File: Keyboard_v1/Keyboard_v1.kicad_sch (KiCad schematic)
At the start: 16 parts, among them SW1 SW_Push, U1 ATmega32U4-A, Y1 16MHz

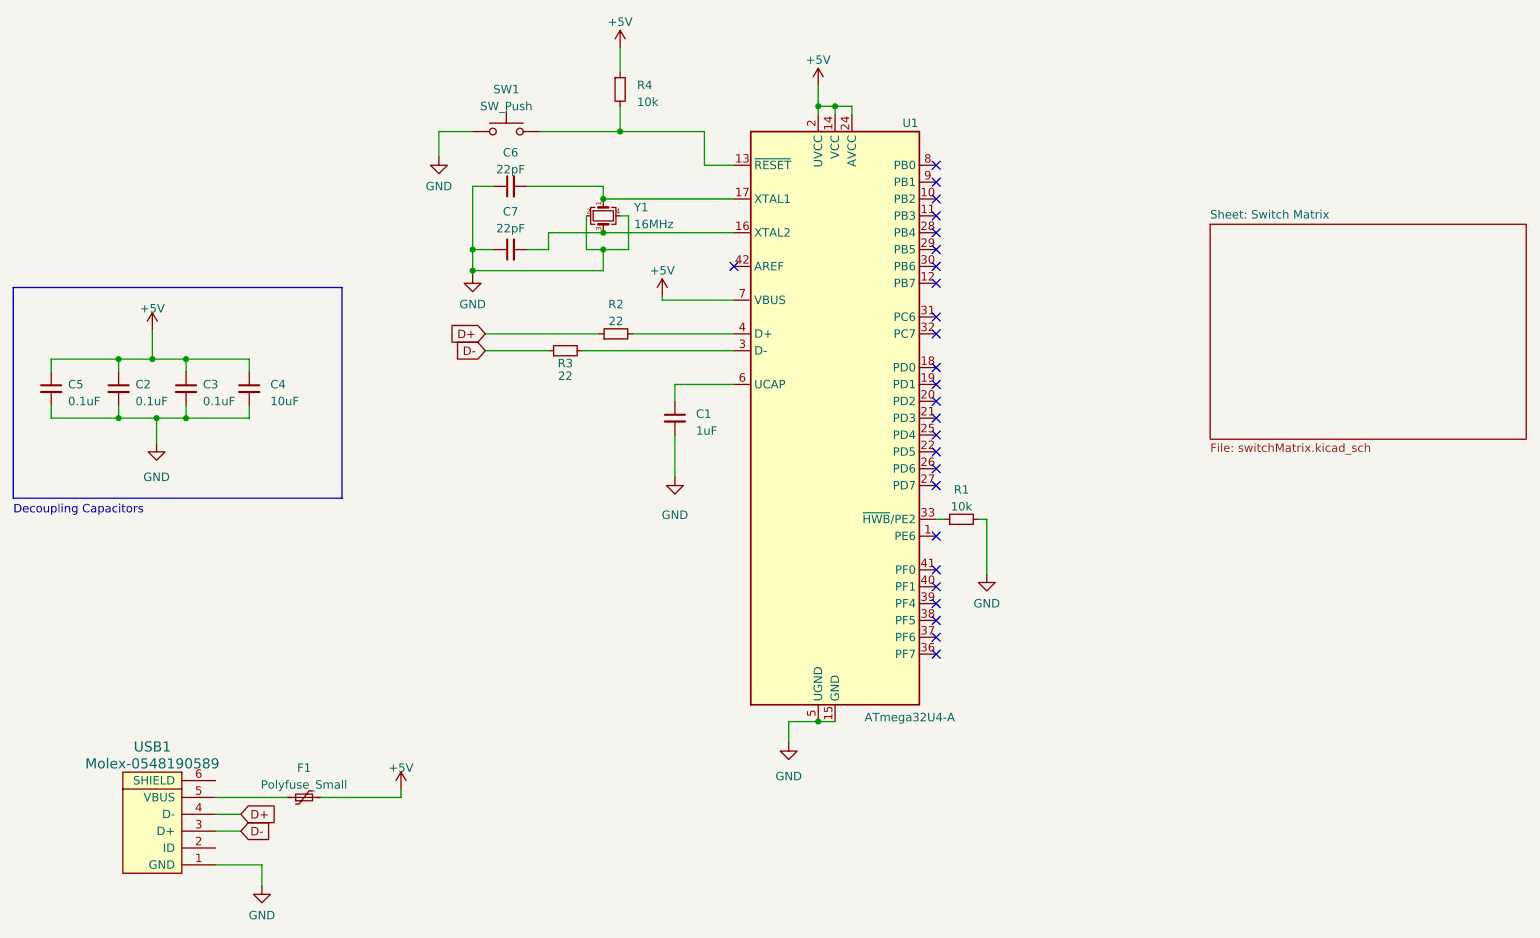
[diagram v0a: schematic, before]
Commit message: key matrix done. placing pcb now
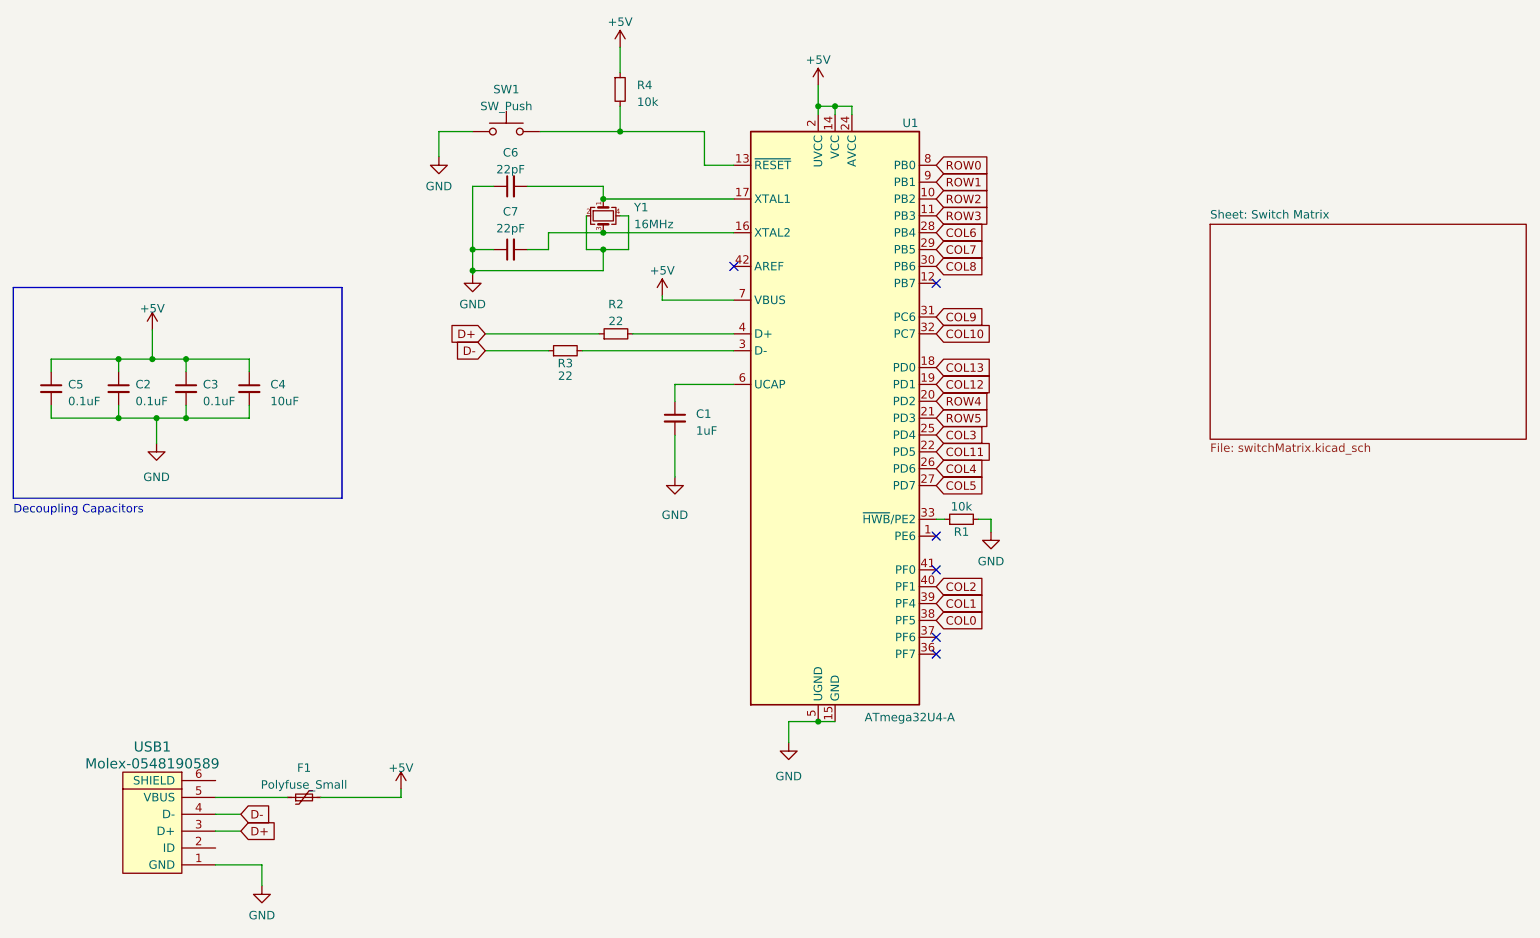
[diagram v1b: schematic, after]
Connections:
- net D+: now also USB1.3 (D+); no longer USB1.4 (D-)
- net D-: now also USB1.4 (D-); no longer USB1.3 (D+)
- net ROW2: now reaches U1.10 (PB2)
- net ROW3: now reaches U1.11 (PB3)
- net COL13: now reaches U1.18 (PD0)
- net COL12: now reaches U1.19 (PD1)
- net ROW4: now reaches U1.20 (PD2)
- net ROW5: now reaches U1.21 (PD3)
- net COL11: now reaches U1.22 (PD5)
- net COL3: now reaches U1.25 (PD4)
- net COL4: now reaches U1.26 (PD6)
- net COL5: now reaches U1.27 (PD7)
- net COL6: now reaches U1.28 (PB4)
- net COL7: now reaches U1.29 (PB5)
- net COL8: now reaches U1.30 (PB6)
- net COL9: now reaches U1.31 (PC6)
- net COL10: now reaches U1.32 (PC7)
- net COL0: now reaches U1.38 (PF5)
- net COL1: now reaches U1.39 (PF4)
- net COL2: now reaches U1.40 (PF1)
- net ROW0: now reaches U1.8 (PB0)
- net ROW1: now reaches U1.9 (PB1)
- no-connect marks 26 -> 6
